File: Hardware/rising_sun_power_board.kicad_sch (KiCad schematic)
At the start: 31 parts, among them J1 Barrel_Jack, J2 Conn_01x03_Socket, J3 Conn_01x03_Socket, SW201 SW_Push, U1 ESP32, U2 MIC5219, U4 TXU0102DCUR, U5 UA78M05IDCYR

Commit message: Final rev1.0 version
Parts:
- U5: value UA78M05IDCYR -> UA78M33IDCYR; Digikey 296-17616-1-ND -> 296-13424-1-ND
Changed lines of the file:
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@@
       (effects (font (size 1.27 1.27)))
     )
-    (property "Value" "UA78M05IDCYR" (at 52.07 78.74 0)
+    (property "Value" "UA78M33IDCYR" (at 52.07 78.74 0)
       (effects (font (size 1.27 1.27)))
     )
@@
       (effects (font (size 1.27 1.27)) hide)
     )
-    (property "Digikey" "296-17616-1-ND" (at 44.45 81.28 0)
+    (property "Digikey" "296-13424-1-ND" (at 44.45 81.28 0)
       (effects (font (size 1.27 1.27)) hide)
     )

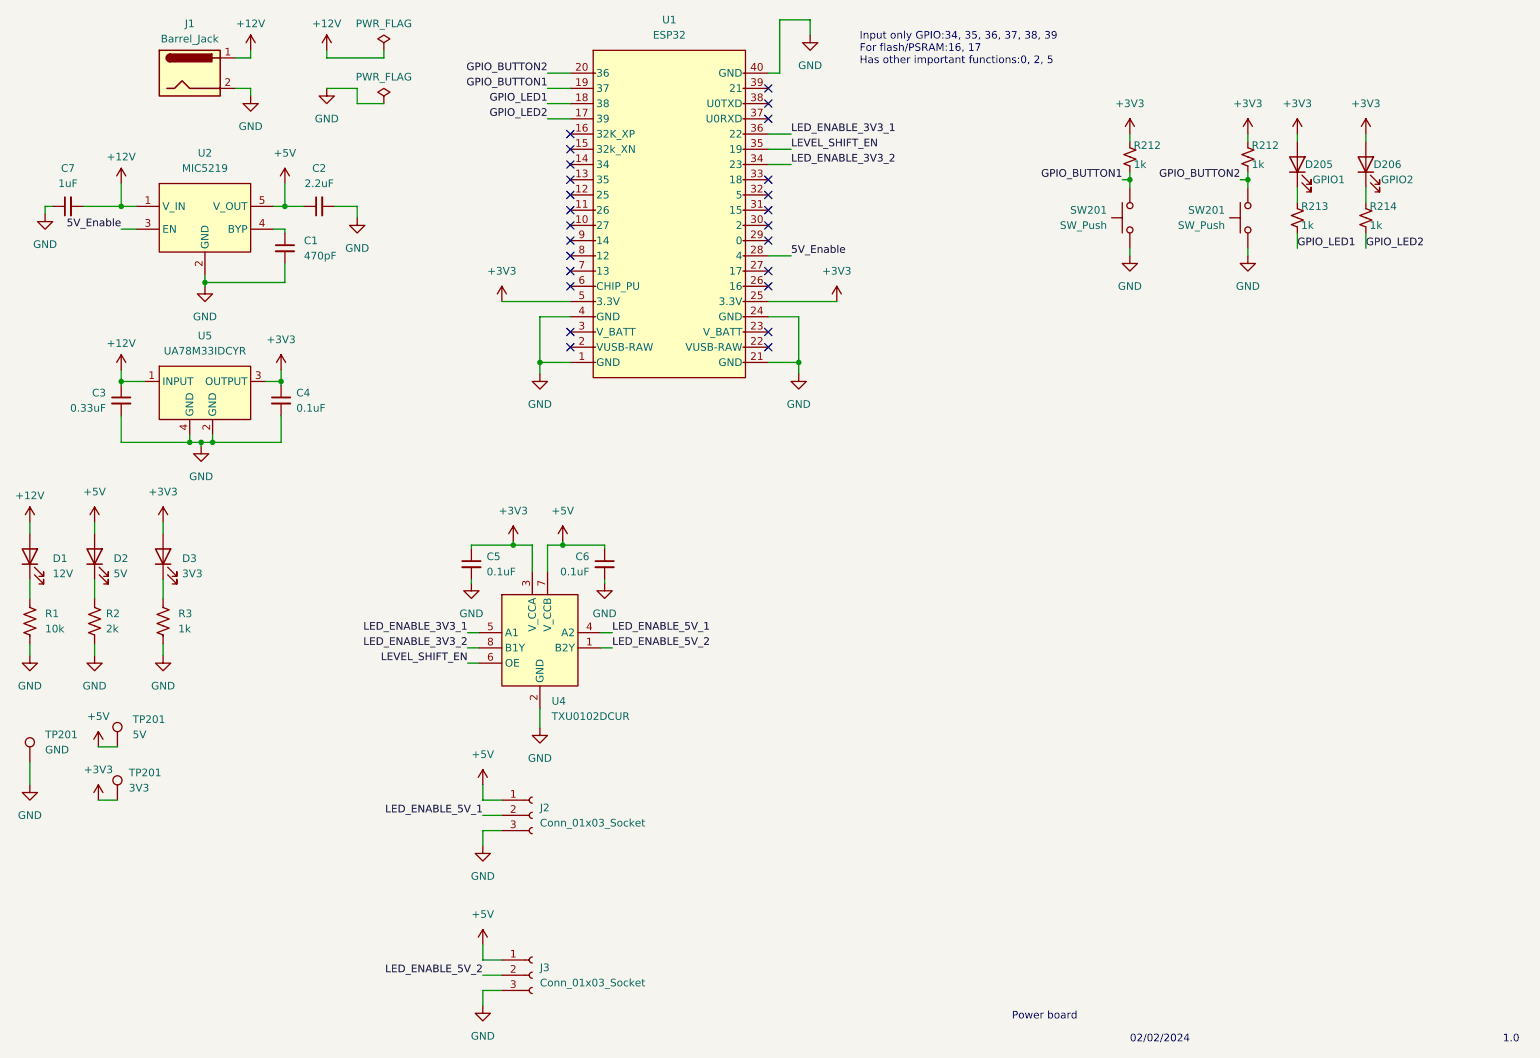
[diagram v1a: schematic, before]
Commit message: fixed some gpios connection
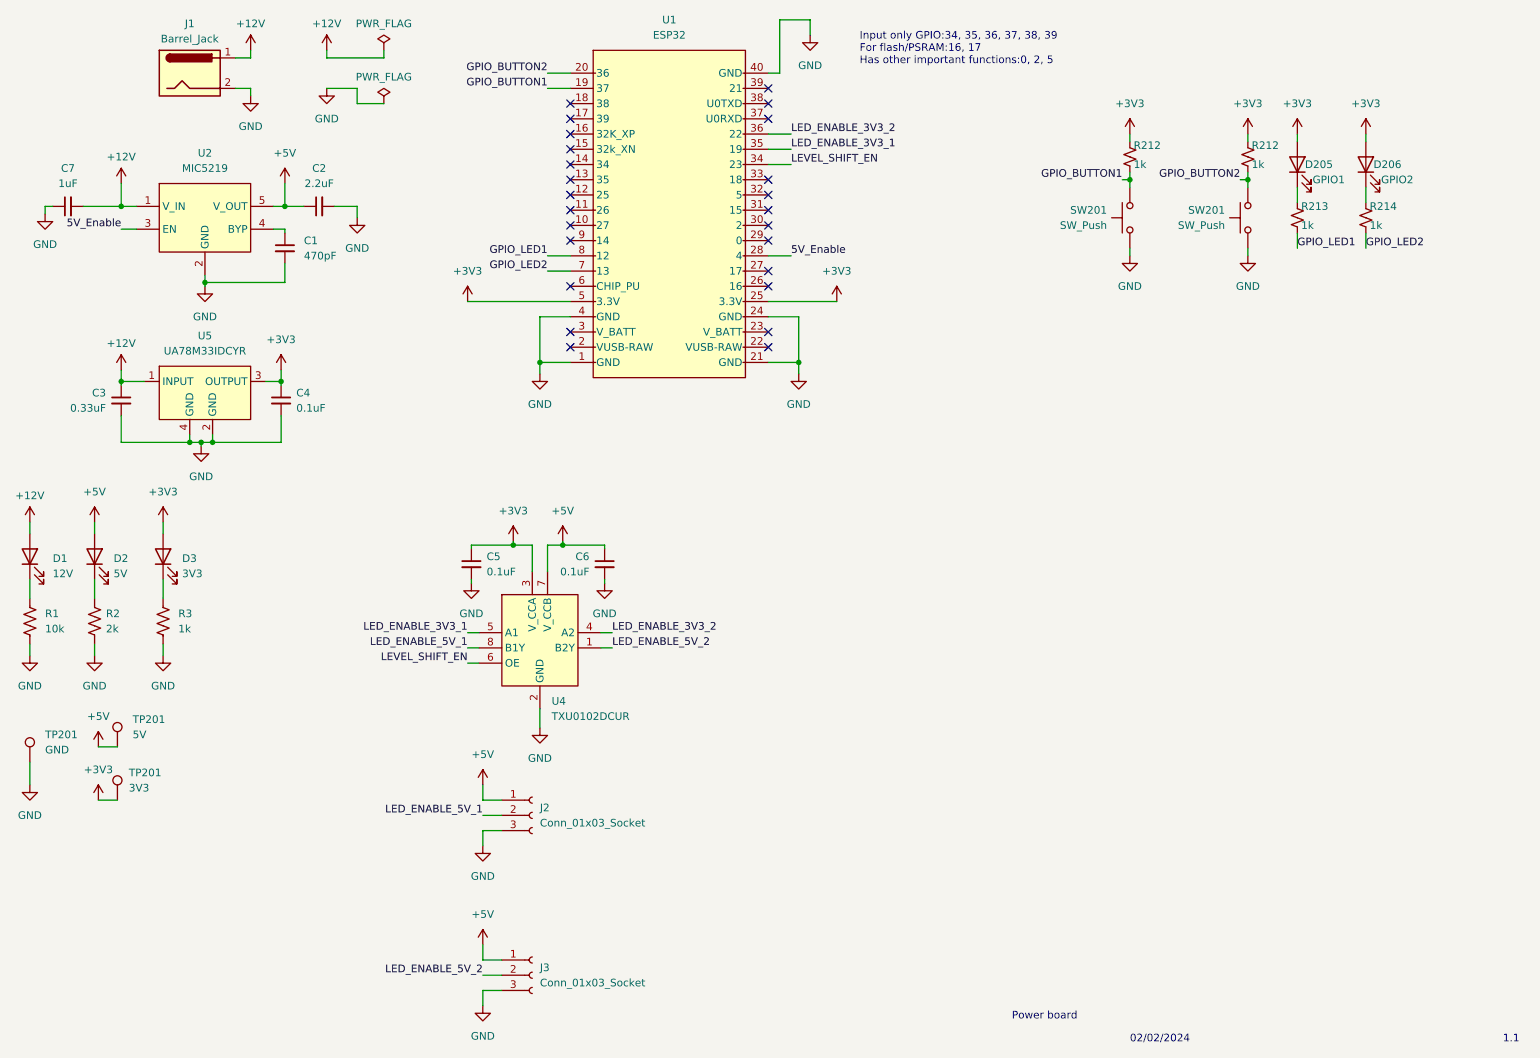
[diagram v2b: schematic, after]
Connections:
- net GPIO_LED1: now also U1.8 (12); no longer U1.18 (38)
- net GPIO_LED2: now also U1.7 (13); no longer U1.17 (39)
- net LED_ENABLE_3V3_1: now also U1.35 (19); no longer U1.36 (22)
- net LED_ENABLE_3V3_2: now also U1.36 (22), U4.4 (A2); no longer U1.34 (23), U4.8 (B1Y)
- net LED_ENABLE_5V_1: now also U4.8 (B1Y); no longer U4.4 (A2)
- net LEVEL_SHIFT_EN: now also U1.34 (23); no longer U1.35 (19)
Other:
- note added: "1.1"
- note removed: "1.0"
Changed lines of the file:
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@@
   (no_connect (at 146.05 65.405))
   (no_connect (at 146.05 75.565))
-  (no_connect (at 113.03 65.405))
+  (no_connect (at 113.03 40.005))
   (no_connect (at 146.05 60.325))
   (no_connect (at 146.05 67.945))
@@
   (no_connect (at 146.05 57.785))
   (no_connect (at 113.03 57.785))
-  (no_connect (at 113.03 62.865))
+  (no_connect (at 113.03 37.465))
   (no_connect (at 113.03 42.545))
   (no_connect (at 146.05 40.005))
@@
     (stroke (width 0) (type default))
   )
-  (wire (pts (xy 101.6 70.485) (xy 113.03 70.485))
-    (stroke (width 0) (type default))
-  )
-  (wire (pts (xy 109.22 37.465) (xy 113.03 37.465))
+  (wire (pts (xy 95.885 70.485) (xy 113.03 70.485))
+    (stroke (width 0) (type default))
+  )
+  (wire (pts (xy 109.22 62.865) (xy 113.03 62.865))
     (stroke (width 0) (type default))
   )
@@
     (stroke (width 0) (type default))
   )
-  (wire (pts (xy 109.22 40.005) (xy 113.03 40.005))
+  (wire (pts (xy 109.22 65.405) (xy 113.03 65.405))
     (stroke (width 0) (type default))
   )
@@
     (effects (font (size 1.27 1.27)) (justify left bottom))
   )
-  (text "1.0\n" (at 268.605 194.31 0)
+  (text "1.1\n" (at 268.605 194.31 0)
     (effects (font (size 1.27 1.27)) (justify left bottom))
   )
@@
     (effects (font (size 1.27 1.27)) (justify right bottom))
   )
-  (label "LED_ENABLE_3V3_2" (at 95.885 128.27 180) (fields_autoplaced)
-    (effects (font (size 1.27 1.27)) (justify right bottom))
+  (label "LED_ENABLE_3V3_2" (at 149.86 42.545 0) (fields_autoplaced)
+    (effects (font (size 1.27 1.27)) (justify left bottom))
   )
   (label "LED_ENABLE_5V_2" (at 120.015 128.27 0) (fields_autoplaced)
@@
     (effects (font (size 1.27 1.27)) (justify right bottom))
   )
+  (label "LED_ENABLE_3V3_2" (at 120.015 125.73 0) (fields_autoplaced)
+    (effects (font (size 1.27 1.27)) (justify left bottom))
+  )
   (label "GPIO_BUTTON2" (at 224.79 50.165 180) (fields_autoplaced)
     (effects (font (size 1.27 1.27)) (justify right bottom))
@@
     (effects (font (size 1.27 1.27)) (justify right bottom))
   )
+  (label "LEVEL_SHIFT_EN" (at 149.86 47.625 0) (fields_autoplaced)
+    (effects (font (size 1.27 1.27)) (justify left bottom))
+  )
   (label "5V_Enable" (at 149.86 62.865 0) (fields_autoplaced)
     (effects (font (size 1.27 1.27)) (justify left bottom))
@@
     (effects (font (size 1.27 1.27)) (justify right bottom))
   )
-  (label "LEVEL_SHIFT_EN" (at 149.86 45.085 0) (fields_autoplaced)
-    (effects (font (size 1.27 1.27)) (justify left bottom))
-  )
   (label "LED_ENABLE_5V_2" (at 98.425 182.88 180) (fields_autoplaced)
     (effects (font (size 1.27 1.27)) (justify right bottom))
   )
-  (label "GPIO_LED2" (at 109.22 40.005 180) (fields_autoplaced)
+  (label "GPIO_LED2" (at 109.22 65.405 180) (fields_autoplaced)
     (effects (font (size 1.27 1.27)) (justify right bottom))
   )
@@
     (effects (font (size 1.27 1.27)) (justify left bottom))
   )
+  (label "LED_ENABLE_3V3_1" (at 149.86 45.085 0) (fields_autoplaced)
+    (effects (font (size 1.27 1.27)) (justify left bottom))
+  )
   (label "GPIO_LED2" (at 245.745 61.595 0) (fields_autoplaced)
     (effects (font (size 1.27 1.27)) (justify left bottom))
   )
-  (label "LED_ENABLE_3V3_2" (at 149.86 47.625 0) (fields_autoplaced)
-    (effects (font (size 1.27 1.27)) (justify left bottom))
-  )
-  (label "LED_ENABLE_5V_1" (at 120.015 125.73 0) (fields_autoplaced)
-    (effects (font (size 1.27 1.27)) (justify left bottom))
-  )
-  (label "GPIO_LED1" (at 109.22 37.465 180) (fields_autoplaced)
+  (label "LED_ENABLE_5V_1" (at 95.885 128.27 180) (fields_autoplaced)
     (effects (font (size 1.27 1.27)) (justify right bottom))
   )
-  (label "LED_ENABLE_3V3_1" (at 149.86 42.545 0) (fields_autoplaced)
-    (effects (font (size 1.27 1.27)) (justify left bottom))
+  (label "GPIO_LED1" (at 109.22 62.865 180) (fields_autoplaced)
+    (effects (font (size 1.27 1.27)) (justify right bottom))
   )
   (symbol (lib_id "Connector:Barrel_Jack") (at 49.53 32.385 0) (unit 1)
@@
     )
   )
-  (symbol (lib_id "power:+3V3") (at 101.6 70.485 0) (unit 1)
-    (in_bom yes) (on_board yes) (dnp no) (fields_autoplaced)
-    (property "Reference" "#PWR06" (at 101.6 74.295 0)
-      (effects (font (size 1.27 1.27)) hide)
-    )
-    (property "Value" "+3V3" (at 101.6 65.405 0)
-      (effects (font (size 1.27 1.27)))
-    )
-    (property "Footprint" "" (at 101.6 70.485 0)
-      (effects (font (size 1.27 1.27)) hide)
-    )
-    (property "Datasheet" "" (at 101.6 70.485 0)
-      (effects (font (size 1.27 1.27)) hide)
-    )
+  (symbol (lib_id "power:+3V3") (at 95.885 70.485 0) (unit 1)
+    (in_bom yes) (on_board yes) (dnp no) (fields_autoplaced)
+    (property "Reference" "#PWR06" (at 95.885 74.295 0)
+      (effects (font (size 1.27 1.27)) hide)
+    )
+    (property "Value" "+3V3" (at 95.885 65.405 0)
+      (effects (font (size 1.27 1.27)))
+    )
+    (property "Footprint" "" (at 95.885 70.485 0)
+      (effects (font (size 1.27 1.27)) hide)
+    )
+    (property "Datasheet" "" (at 95.885 70.485 0)
+      (effects (font (size 1.27 1.27)) hide)
+    )
